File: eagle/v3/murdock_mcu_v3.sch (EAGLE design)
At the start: 34 parts, among them IC1 MPU-9150, IC2 LT1763CS8-3.3, IC3 STM32F4XX_64, IC4 BMP085, IC5 24LC16BSN, T1 PFET, U1 USD-SOCKETNEW, X2 MURDOCK_STACK

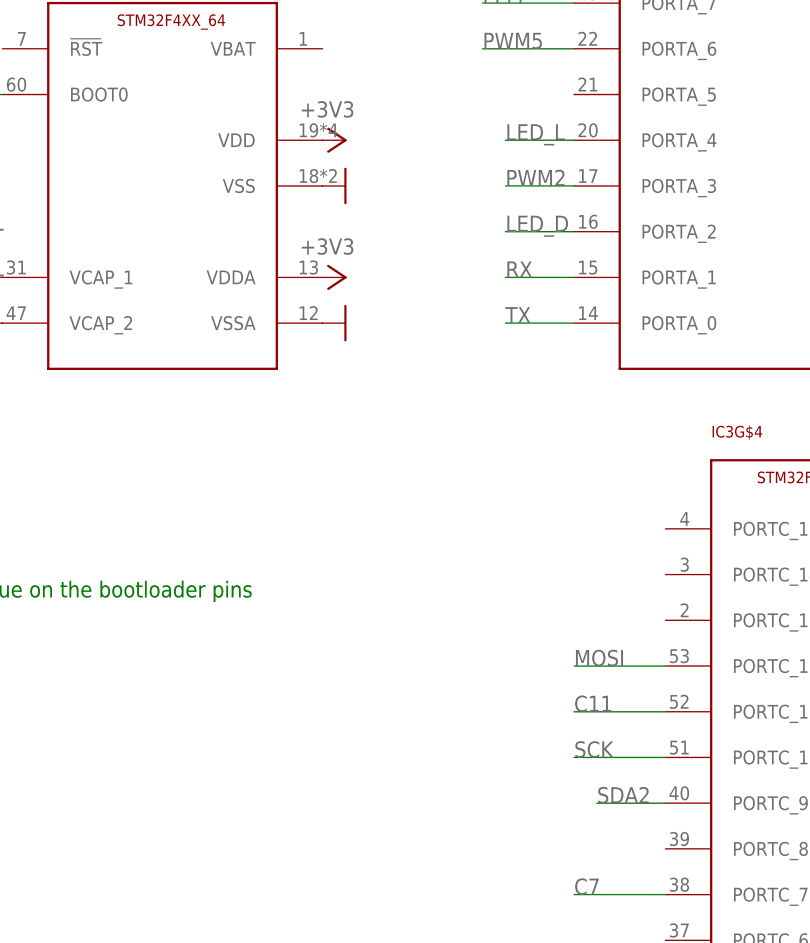
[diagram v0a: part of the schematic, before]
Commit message: invert sbus
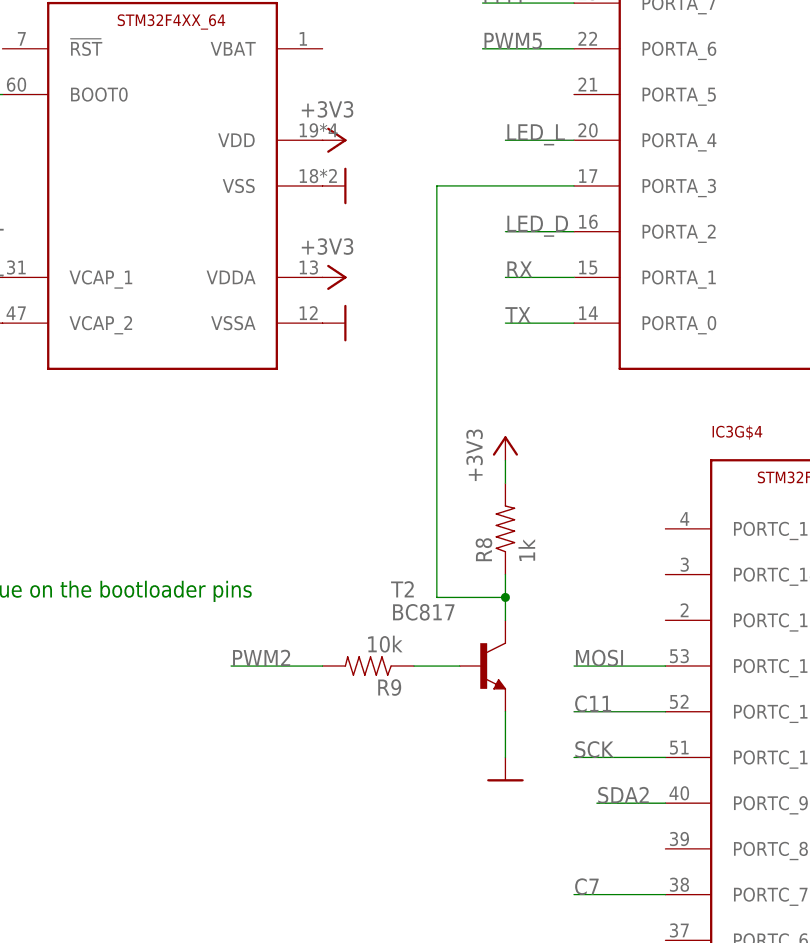
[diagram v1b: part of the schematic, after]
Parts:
- added R8: 1k, SparkFun-Resistors:RESISTOR0402-RES
- added R9: 10k, SparkFun-Resistors:RESISTOR0402-RES
- added T2: BC817, transistor:BC847
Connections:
- new net N$11: IC3G$2.PORTA_3, R8.1, T2.C
- new net N$12: R9.1, T2.B
- net +3V3: now also R8.2
- net GND: now also T2.E
- net PWM2: now also R9.2; no longer IC3G$2.PORTA_3
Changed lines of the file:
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@@
 <part name="R7" library="SparkFun-Resistors" deviceset="RESISTOR" device="0402-RES" value="15k"/>
 <part name="P+4" library="supply1" deviceset="+5V" device=""/>
+<part name="T2" library="transistor" deviceset="BC847" device="" value="BC817"/>
+<part name="+3V14" library="supply1" deviceset="+3V3" device=""/>
+<part name="GND30" library="SparkFun-Aesthetics" deviceset="GND" device=""/>
+<part name="R8" library="SparkFun-Resistors" deviceset="RESISTOR" device="0402-RES" value="1k"/>
+<part name="R9" library="SparkFun-Resistors" deviceset="RESISTOR" device="0402-RES" value="10k"/>
 </parts>
 <sheets>
@@
 <instance part="R7" gate="G$1" x="78.74" y="-10.16" rot="R180"/>
 <instance part="P+4" gate="1" x="-30.48" y="137.16" rot="R90"/>
+<instance part="T2" gate="G$1" x="-27.94" y="53.34"/>
+<instance part="+3V14" gate="G$1" x="-25.4" y="78.74"/>
+<instance part="GND30" gate="1" x="-25.4" y="40.64" smashed="yes"/>
+<instance part="R8" gate="G$1" x="-25.4" y="68.58" rot="R90"/>
+<instance part="R9" gate="G$1" x="-40.64" y="53.34" rot="R180"/>
 </instances>
 <busses>
@@
 <wire x1="111.76" y1="104.14" x2="111.76" y2="109.22" width="0.1524" layer="91"/>
 </segment>
+<segment>
+<wire x1="-25.4" y1="48.26" x2="-25.4" y2="43.18" width="0.1524" layer="91"/>
+<pinref part="T2" gate="G$1" pin="E"/>
+<pinref part="GND30" gate="1" pin="GND"/>
+</segment>
 </net>
 <net name="+3V3" class="0">
@@
 <wire x1="132.08" y1="132.08" x2="132.08" y2="127" width="0.1524" layer="91"/>
 </segment>
+<segment>
+<wire x1="-25.4" y1="73.66" x2="-25.4" y2="76.2" width="0.1524" layer="91"/>
+<pinref part="+3V14" gate="G$1" pin="+3V3"/>
+<pinref part="R8" gate="G$1" pin="2"/>
+</segment>
 </net>
 <net name="+5V" class="0">
@@
 </segment>
 <segment>
-<pinref part="IC3" gate="G$2" pin="PORTA_3"/>
-<wire x1="-17.78" y1="106.68" x2="-25.4" y2="106.68" width="0.1524" layer="91"/>
-<label x="-25.4" y="106.68" size="1.778" layer="95"/>
+<wire x1="-55.88" y1="53.34" x2="-45.72" y2="53.34" width="0.1524" layer="91"/>
+<label x="-55.88" y="53.34" size="1.778" layer="95"/>
+<pinref part="R9" gate="G$1" pin="2"/>
 </segment>
 </net>
@@
 </segment>
 </net>
+<net name="N$12" class="0">
+<segment>
+<wire x1="-35.56" y1="53.34" x2="-30.48" y2="53.34" width="0.1524" layer="91"/>
+<pinref part="T2" gate="G$1" pin="B"/>
+<pinref part="R9" gate="G$1" pin="1"/>
+</segment>
+</net>
+<net name="N$11" class="0">
+<segment>
+<pinref part="T2" gate="G$1" pin="C"/>
+<wire x1="-25.4" y1="58.42" x2="-25.4" y2="60.96" width="0.1524" layer="91"/>
+<wire x1="-25.4" y1="60.96" x2="-25.4" y2="63.5" width="0.1524" layer="91"/>
+<wire x1="-25.4" y1="60.96" x2="-33.02" y2="60.96" width="0.1524" layer="91"/>
+<wire x1="-33.02" y1="60.96" x2="-33.02" y2="106.68" width="0.1524" layer="91"/>
+<junction x="-25.4" y="60.96"/>
+<pinref part="IC3" gate="G$2" pin="PORTA_3"/>
+<wire x1="-33.02" y1="106.68" x2="-17.78" y2="106.68" width="0.1524" layer="91"/>
+<pinref part="R8" gate="G$1" pin="1"/>
+</segment>
+</net>
